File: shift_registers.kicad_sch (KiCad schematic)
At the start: 2 parts

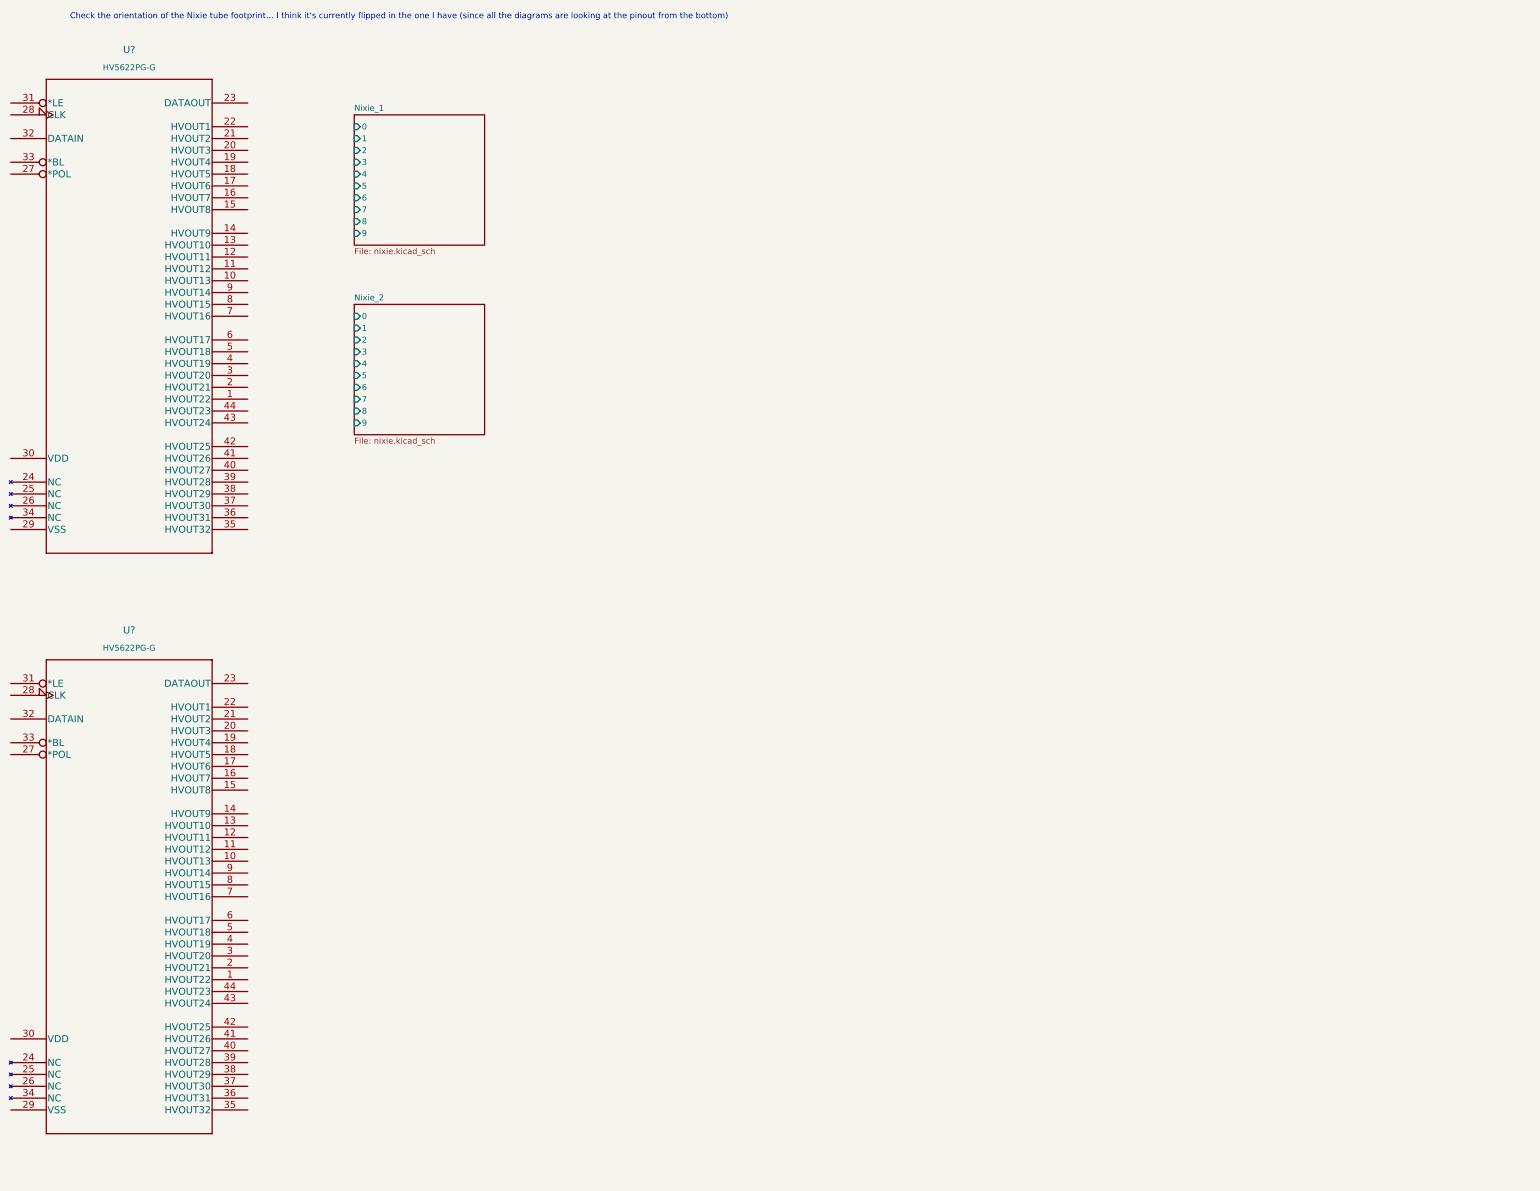
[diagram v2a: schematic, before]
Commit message: wired up Nixie tubes
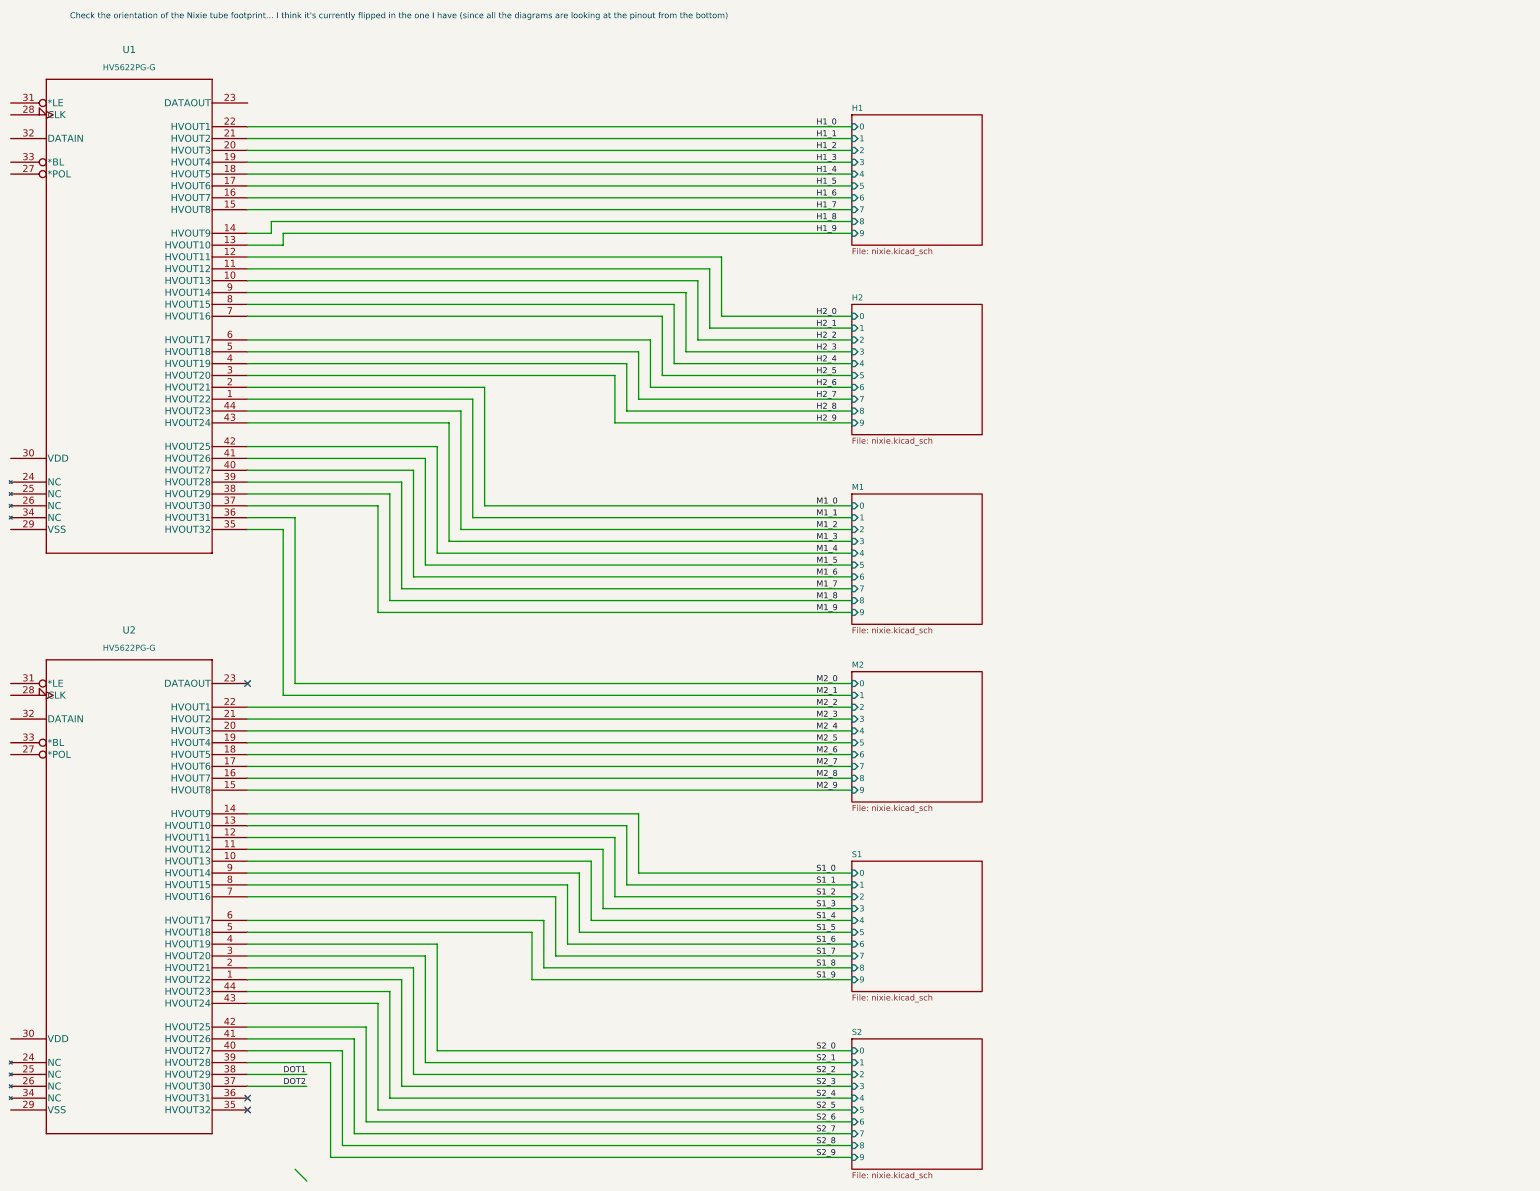
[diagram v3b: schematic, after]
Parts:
- gave numbers to parts that had none: 2
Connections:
- net S2_3: now reaches U2.1 (HVOUT22)
- net S1_4: now reaches U2.10 (HVOUT13)
- net S1_3: now reaches U2.11 (HVOUT12)
- net S1_2: now reaches U2.12 (HVOUT11)
- net S1_1: now reaches U2.13 (HVOUT10)
- net S1_0: now reaches U2.14 (HVOUT9)
- net M2_9: now reaches U2.15 (HVOUT8)
- net M2_8: now reaches U2.16 (HVOUT7)
- net M2_7: now reaches U2.17 (HVOUT6)
- net M2_6: now reaches U2.18 (HVOUT5)
- net M2_5: now reaches U2.19 (HVOUT4)
- net S2_2: now reaches U2.2 (HVOUT21)
- net M2_4: now reaches U2.20 (HVOUT3)
- net M2_3: now reaches U2.21 (HVOUT2)
- net M2_2: now reaches U2.22 (HVOUT1)
- net S2_1: now reaches U2.3 (HVOUT20)
- net DOT2: now reaches U2.37 (HVOUT30)
- net DOT1: now reaches U2.38 (HVOUT29)
- net S2_9: now reaches U2.39 (HVOUT28)
- net S2_0: now reaches U2.4 (HVOUT19)
- net S2_8: now reaches U2.40 (HVOUT27)
- net S2_7: now reaches U2.41 (HVOUT26)
- net S2_6: now reaches U2.42 (HVOUT25)
- net S2_5: now reaches U2.43 (HVOUT24)
- net S2_4: now reaches U2.44 (HVOUT23)
- net S1_9: now reaches U2.5 (HVOUT18)
- net S1_8: now reaches U2.6 (HVOUT17)
- net S1_7: now reaches U2.7 (HVOUT16)
- net S1_6: now reaches U2.8 (HVOUT15)
- net S1_5: now reaches U2.9 (HVOUT14)
- net M1_1: now reaches U1.1 (HVOUT22)
- net H2_2: now reaches U1.10 (HVOUT13)
- net H2_1: now reaches U1.11 (HVOUT12)
- net H2_0: now reaches U1.12 (HVOUT11)
- net H1_9: now reaches U1.13 (HVOUT10)
- net H1_8: now reaches U1.14 (HVOUT9)
- net H1_7: now reaches U1.15 (HVOUT8)
- net H1_6: now reaches U1.16 (HVOUT7)
- net H1_5: now reaches U1.17 (HVOUT6)
- net H1_4: now reaches U1.18 (HVOUT5)
- net H1_3: now reaches U1.19 (HVOUT4)
- net M1_0: now reaches U1.2 (HVOUT21)
- net H1_2: now reaches U1.20 (HVOUT3)
- net H1_1: now reaches U1.21 (HVOUT2)
- net H1_0: now reaches U1.22 (HVOUT1)
- net H2_9: now reaches U1.3 (HVOUT20)
- net M2_1: now reaches U1.35 (HVOUT32)
- net M2_0: now reaches U1.36 (HVOUT31)
- net M1_9: now reaches U1.37 (HVOUT30)
- net M1_8: now reaches U1.38 (HVOUT29)
- net M1_7: now reaches U1.39 (HVOUT28)
- net H2_8: now reaches U1.4 (HVOUT19)
- net M1_6: now reaches U1.40 (HVOUT27)
- net M1_5: now reaches U1.41 (HVOUT26)
- net M1_4: now reaches U1.42 (HVOUT25)
- net M1_3: now reaches U1.43 (HVOUT24)
- net M1_2: now reaches U1.44 (HVOUT23)
- net H2_7: now reaches U1.5 (HVOUT18)
- net H2_6: now reaches U1.6 (HVOUT17)
- net H2_5: now reaches U1.7 (HVOUT16)
- net H2_4: now reaches U1.8 (HVOUT15)
- net H2_3: now reaches U1.9 (HVOUT14)
- no-connect marks 0 -> 3
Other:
- sheet Nixie_1 renamed H1
- sheet Nixie_2 renamed H2
- added sheet M1 (nixie.kicad_sch)
- added sheet M2 (nixie.kicad_sch)
- added sheet S1 (nixie.kicad_sch)
- added sheet S2 (nixie.kicad_sch)
